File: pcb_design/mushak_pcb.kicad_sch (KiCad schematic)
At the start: 47 parts, among them J1 Conn_01x04_Male, J10 IR_1, J11 AS5600_1, J12 IR_2, J13 AS5600_2, J14 IR_3, J15 ToF, J16 IR_4, J2 Conn_01x02_Female, J3 BLE_Conn, Q1 DMN3065LW-7, SW1 SW_Push, SW2 SW_Push, U1 AMS1117-3.3, U6 STM32F405RGTx, Y1 25Mhz, Y2 32.769kHz

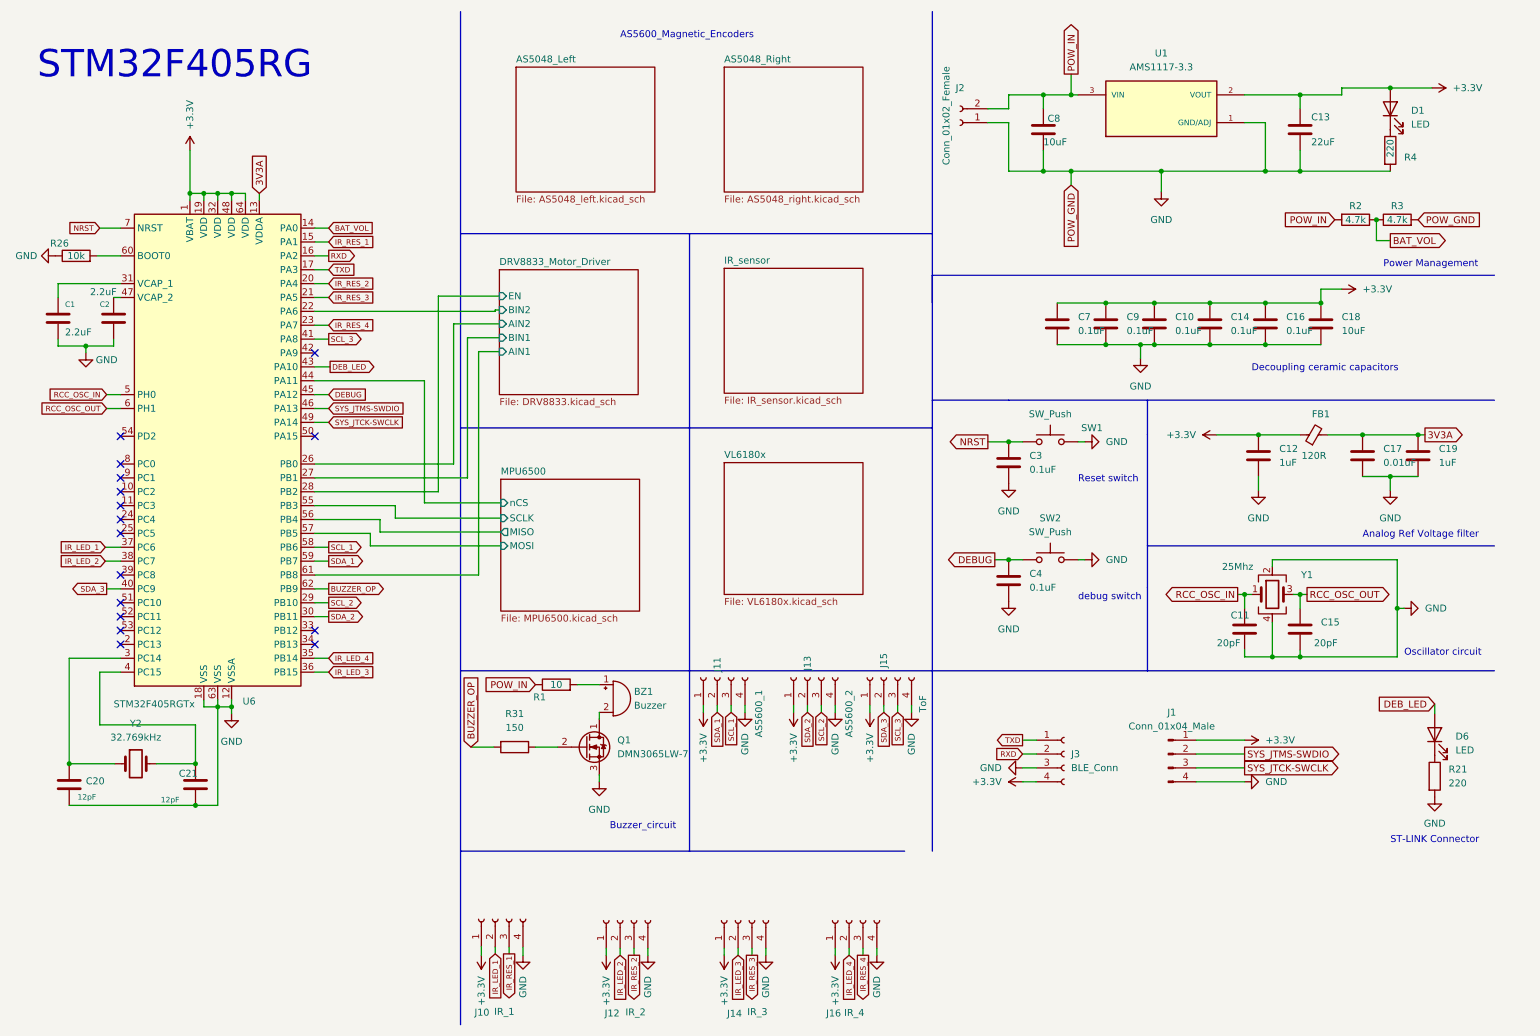
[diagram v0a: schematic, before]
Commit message: Add changes to silkscreen and filter capacitors
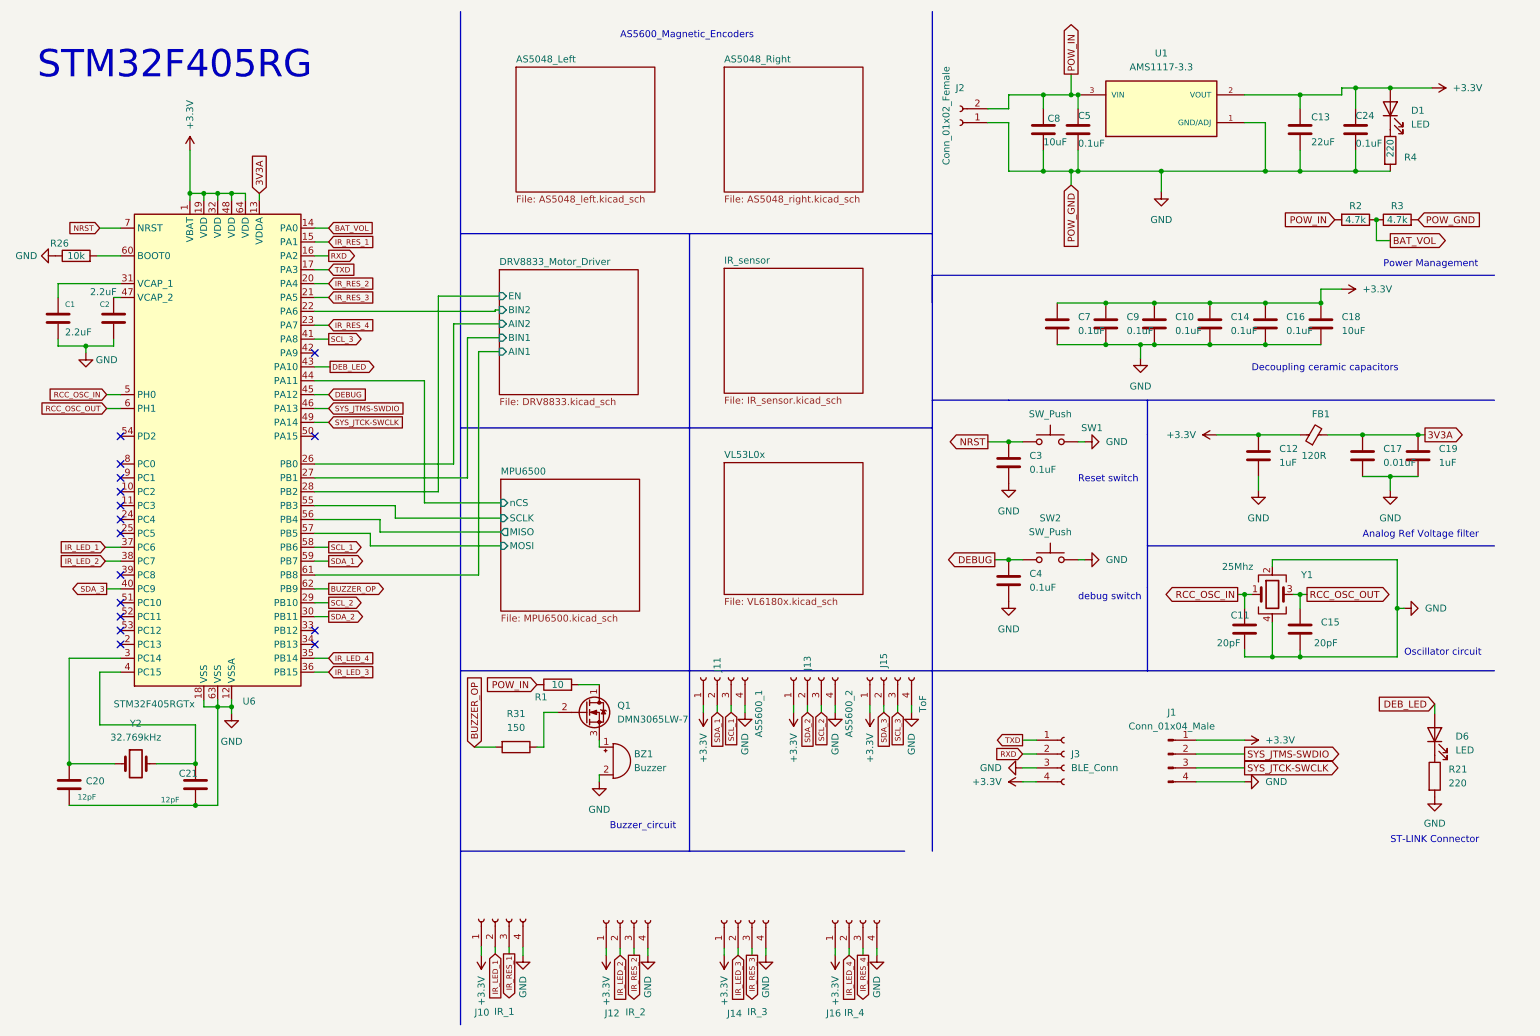
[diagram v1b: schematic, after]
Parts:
- added C24, C5: 0.1uF, Capacitor_SMD:C_0402_1005Metric, symbol Device:C
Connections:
- net +3.3V: now also C24.1
- net GND: now also BZ1.2 (+), C24.2, C5.2; no longer Q1.3 (S)
- net POW_IN: now also C5.1
- net at R1.2: now also Q1.1 (D); no longer BZ1.1 (-)
- new net: BZ1.1 (-), Q1.3 (S)
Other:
- sheet VL6180x renamed VL53L0x
- moved on the sheet: BZ1, Q1
